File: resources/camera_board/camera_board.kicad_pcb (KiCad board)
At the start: 2 copper layers, 94 x 66 mm, 10 parts, among them P1 CONN_01X02

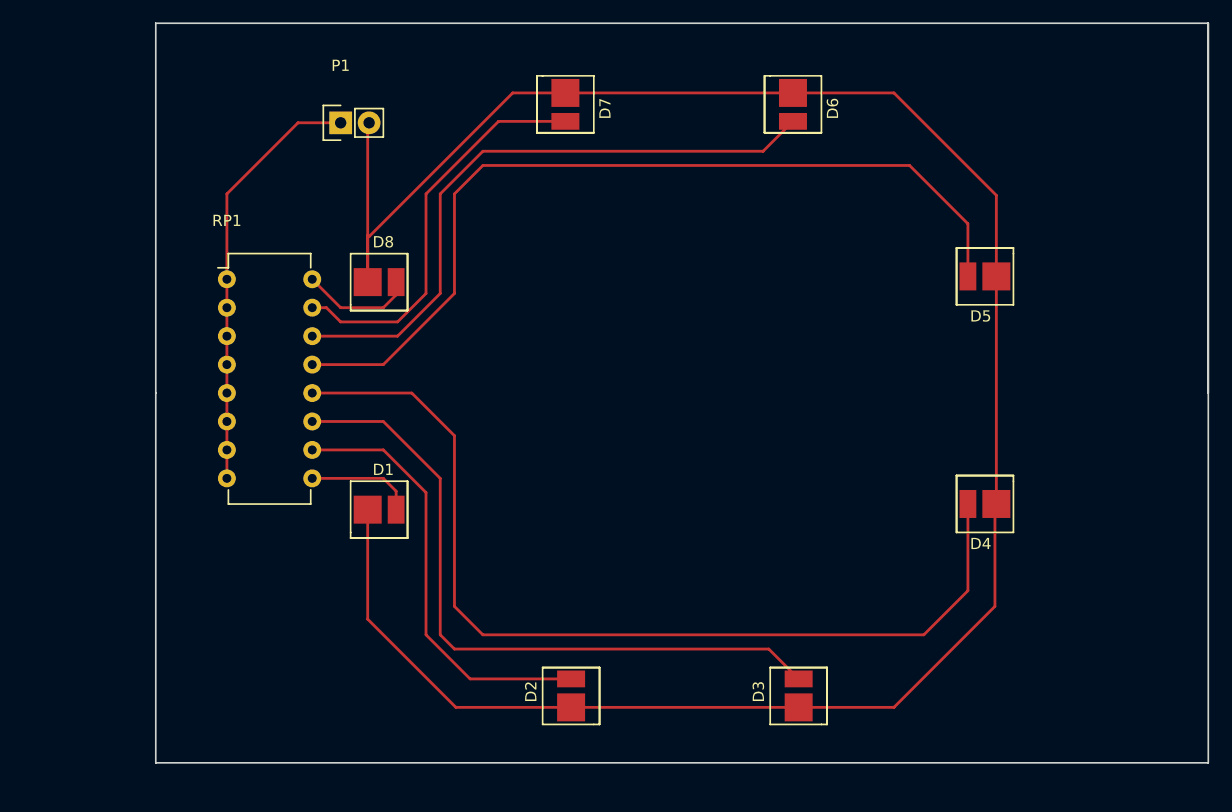
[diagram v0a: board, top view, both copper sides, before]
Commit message: added new pcb version of camera board for wired leds
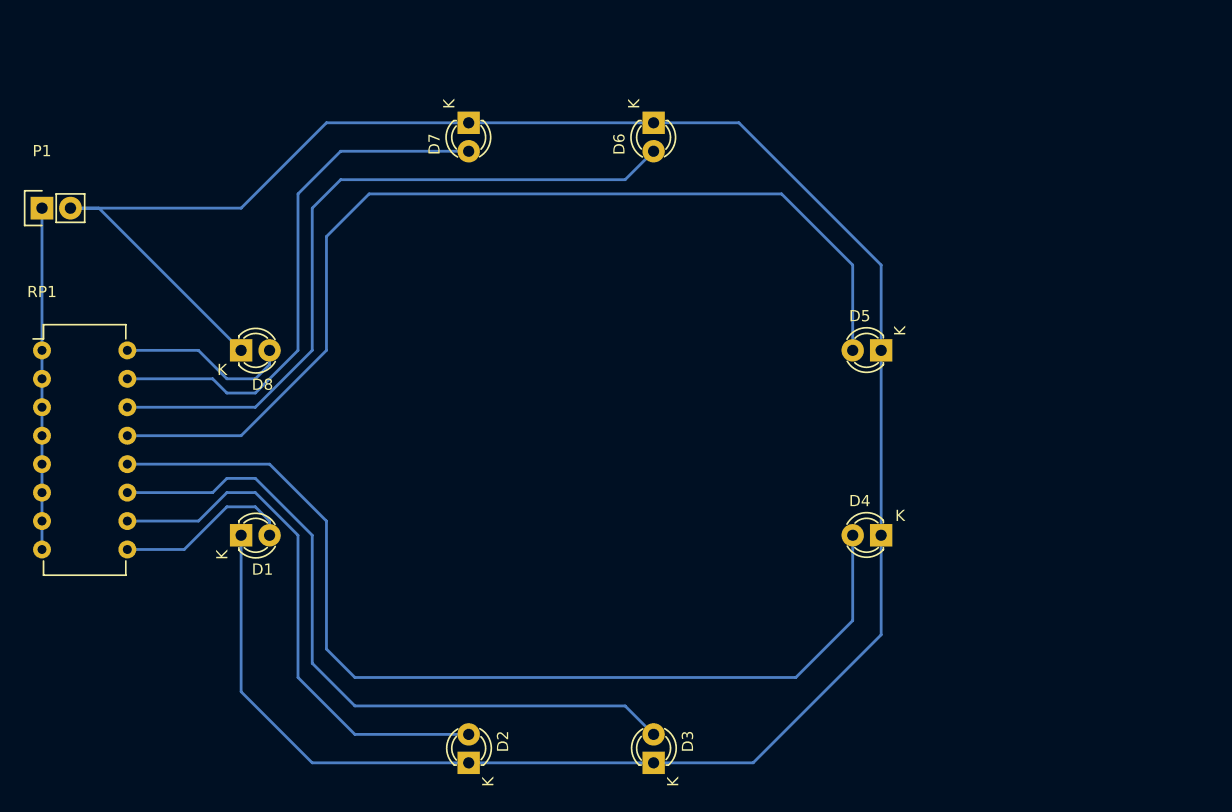
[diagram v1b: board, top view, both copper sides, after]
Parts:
- D1, D2, D3, D4, D5, D6, D7, D8: footprint custom:LED_SMD_5050 -> LEDs:LED-3MM
- moved P1 27.7 mm to (78.7, 68.6)
- moved RP1 17.7 mm to (78.7, 81.3)
- moved D6 16.6 mm to (133.3, 61.0)
- moved D8 16.3 mm to (96.5, 81.3)
- moved D1 14.2 mm to (96.5, 97.8)
- moved D7 12.8 mm to (116.8, 61.0)
- moved D3 10.9 mm to (133.3, 118.1)
- moved D5 9.25 mm to (153.7, 81.3)
- moved D4 8.98 mm to (153.7, 97.8)
- moved D2 8.13 mm to (116.8, 118.1)
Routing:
- net GND: track 193.2 -> 212.8 mm
- net Net-(D7-Pad2): track 35.8 -> 48.1 mm
- net Net-(D5-Pad2): track 78.0 -> 89.9 mm
- net Net-(D2-Pad2): track 39.0 -> 47.9 mm
- net Net-(D6-Pad2): track 56.1 -> 63.9 mm
- net +5V: track 38.2 -> 30.5 mm
- net Net-(D1-Pad2): track 9.62 -> 16.1 mm
- net Net-(D8-Pad2): track 10.2 -> 15.5 mm
- net Net-(D4-Pad2): track 85.8 -> 89.1 mm
- net Net-(D3-Pad2): track 61.1 -> 63.7 mm
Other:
- board outline removed
- rule pad_to_mask_clearance: 0.2 -> 0
- board text added: "Hybrid Letterbox Camera Board v1.1"
